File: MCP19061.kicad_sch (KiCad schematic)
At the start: 47 parts, among them J9 ENABLE_JMP

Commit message: Update
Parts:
- removed J9: ENABLE_JMP, Connector_PinHeader_2.54mm:PinHeader_1x03_P2.54mm_Vertical, symbol Connector_Generic:Conn_01x03
- removed R61, R62, R63, R64: 4k7, Resistor_SMD:R_0805_2012Metric, symbol Device:R
- added R4: 4k7, Resistor_SMD:R_0805_2012Metric, symbol Device:R
- MS1, MS2, MS3, MS4: footprint Package_SON:Infineon_PG-TDSON-8_6.15x5.15mm -> IPC100N04S51R2ATMA1
- R33, R35: value 5m_1% -> 5m_1%_CRE2512-FZ-R005E-2; footprint Resistor_SMD:R_0805_2012Metric -> Resistor_SMD:R_2512_6332Metric
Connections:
- net +3.3V: now also C50.1, SMPS1.8 (VDD_IO), R4.1
- net +5V: no longer C32.1, C50.1, SMPS1.14 (VIN), SMPS1.8 (VDD_IO)
- net +VIN_SMPS: now also C32.1, SMPS1.14 (VIN)
- net +VOUT_SMPS: now also R35.2; no longer R35.1
- net ENABLE: now also R4.2
- net D_MS2: now reaches L2.1, MS1.1 (S_1), MS1.2 (S_2), MS1.3 (S_3), MS2.5 (D_4)
- net D_MS2: no longer MS2.6 (D_2), MS2.7 (D_3), MS2.8 (D_4)
- net D_MS1: now reaches MS1.5 (D_4), R32.1, R33.2
- net D_MS1: no longer MS1.6 (D_2), MS1.7 (D_3), MS1.8 (D_4)
- net D_MS4: now reaches L2.2, MS3.1 (S_1), MS3.2 (S_2), MS3.3 (S_3), MS4.5 (D_4)
- net D_MS4: no longer MS4.6 (D_2), MS4.7 (D_3), MS4.8 (D_4)
- new net D_MS3: MS3.5 (D_4), R35.1, R36.1
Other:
- note added: "GMK316AB7106KL-TR 10uF, 35V, X7R"
- note added: "Receiving MCU has internal pull-ups"
- moved on the sheet: R35

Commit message: Update
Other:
- company: (none) -> Peter Hancak
- title: (none) -> USB-PD Board
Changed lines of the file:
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@@
 	(generator_version "8.0")
 	(paper "USLetter")
+	(title_block
+		(title "USB-PD Board")
+		(date "2025-12-03")
+		(rev "B")
+		(company "Peter Hancak")
+	)

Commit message: Update
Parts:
- R65: value 4k7 -> 10k
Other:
- note added: "Sets I2C Addr (hex) to 0x53 (10k R on ADR0)"

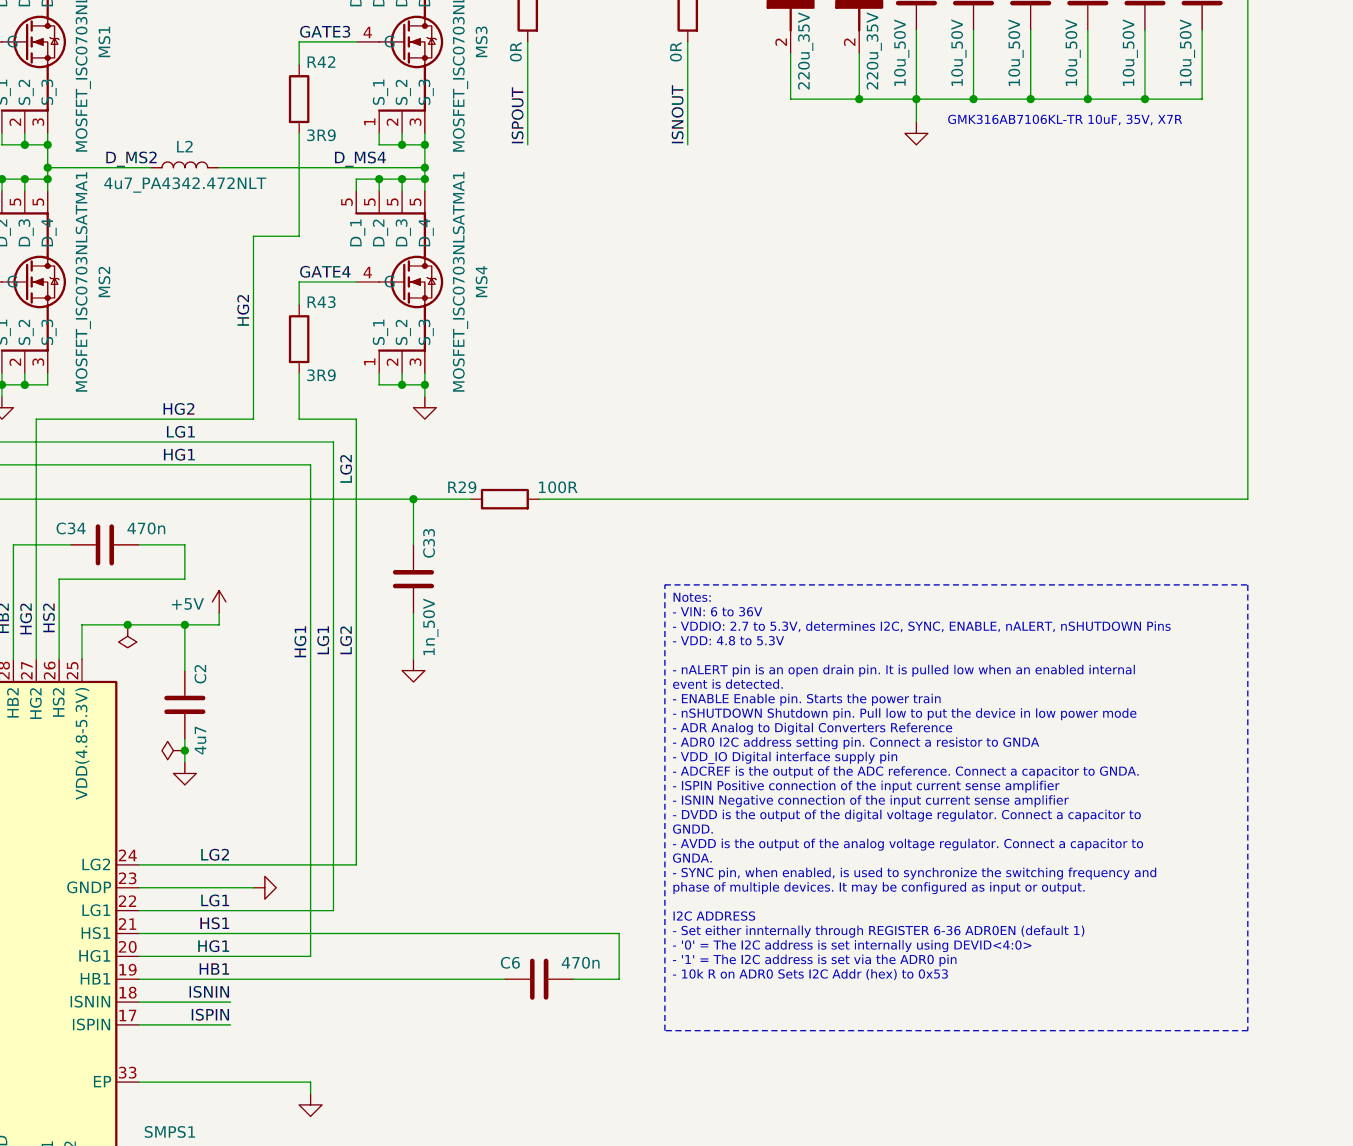
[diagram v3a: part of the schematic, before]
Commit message: Change Kicad version
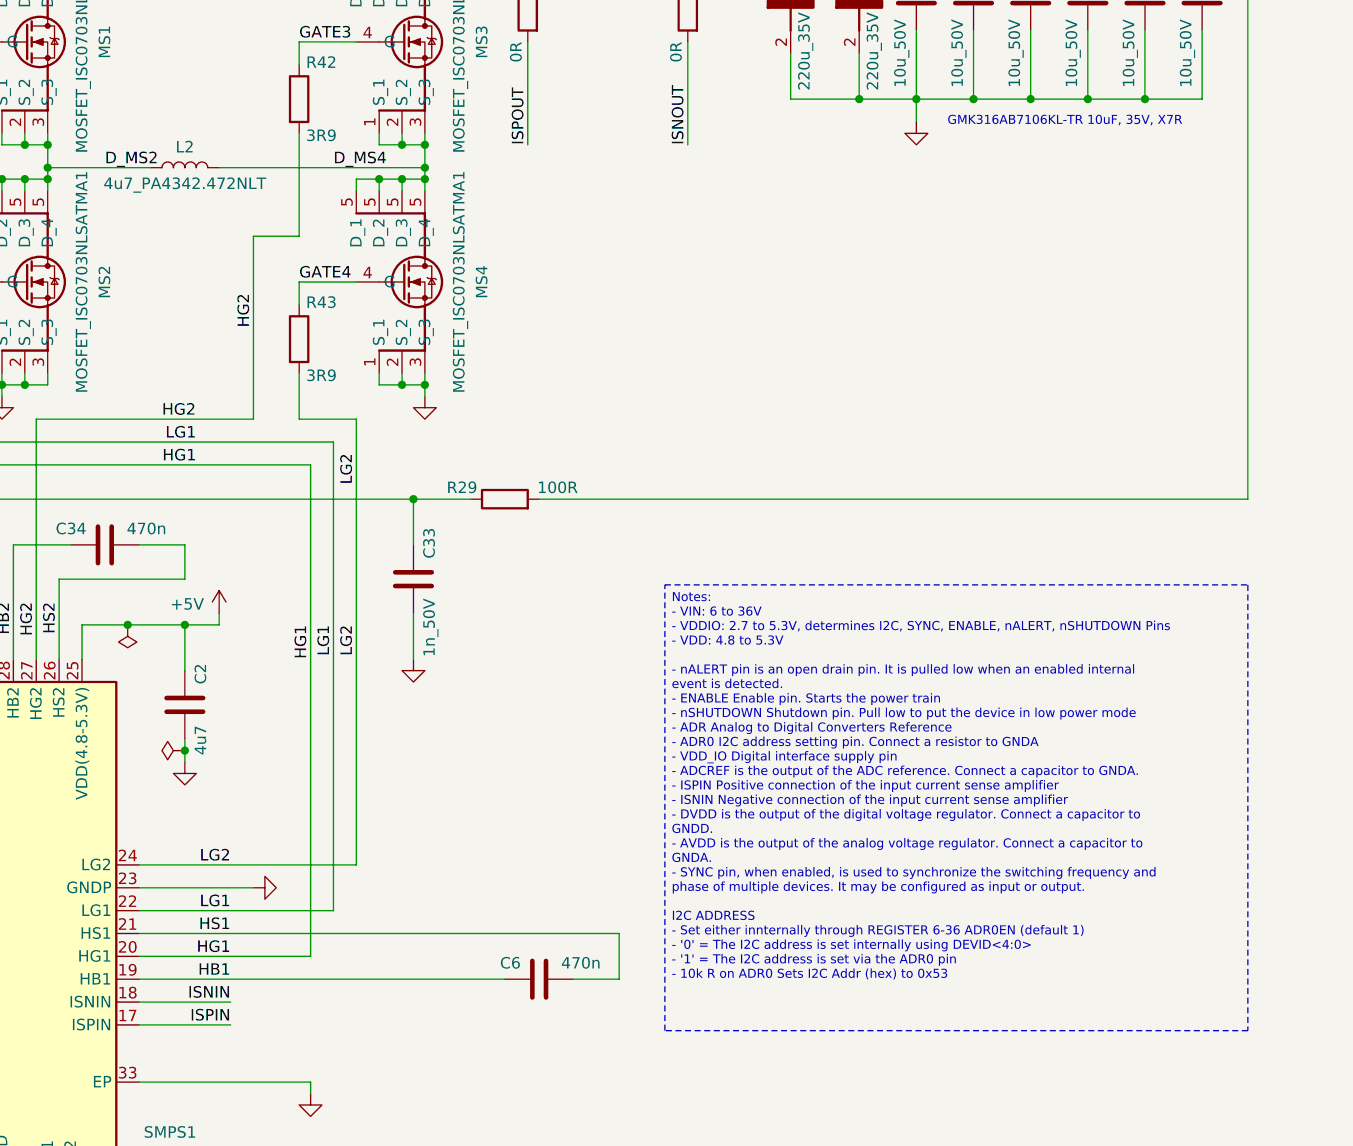
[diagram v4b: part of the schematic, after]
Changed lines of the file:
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@@
 (kicad_sch
-	(version 20231120)
+	(version 20260306)
 	(generator "eeschema")
-	(generator_version "8.0")
+	(generator_version "10.0")
 	(paper "USLetter")
 	(title_block
